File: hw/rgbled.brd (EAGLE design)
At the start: 100 x 80 mm, 17 parts, among them IC1 LE33CZ, Q1 IRLZ34N, Q2 IRLZ34N, Q3 IRLZ34N, U1 ATTINY85-20P, X1 22-23-2021

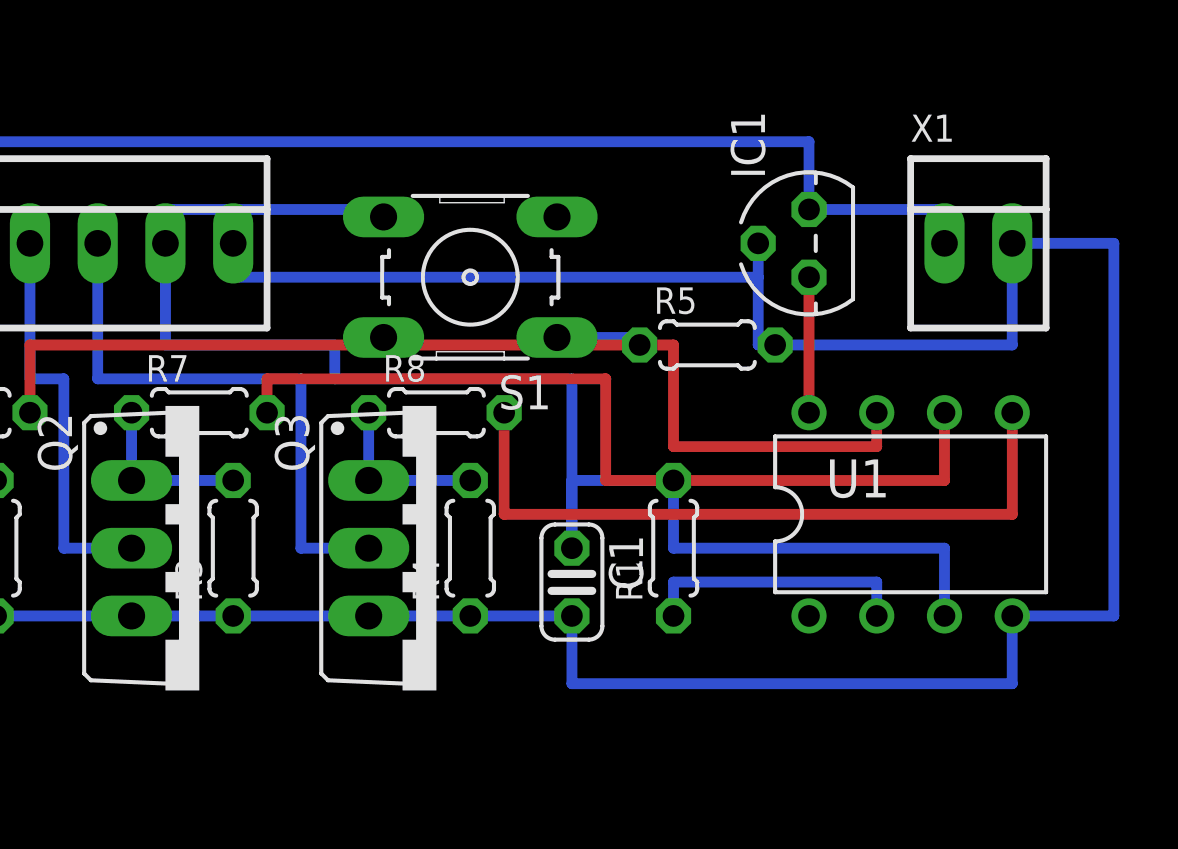
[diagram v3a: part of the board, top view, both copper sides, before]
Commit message: vyhozen dotykovy senzor
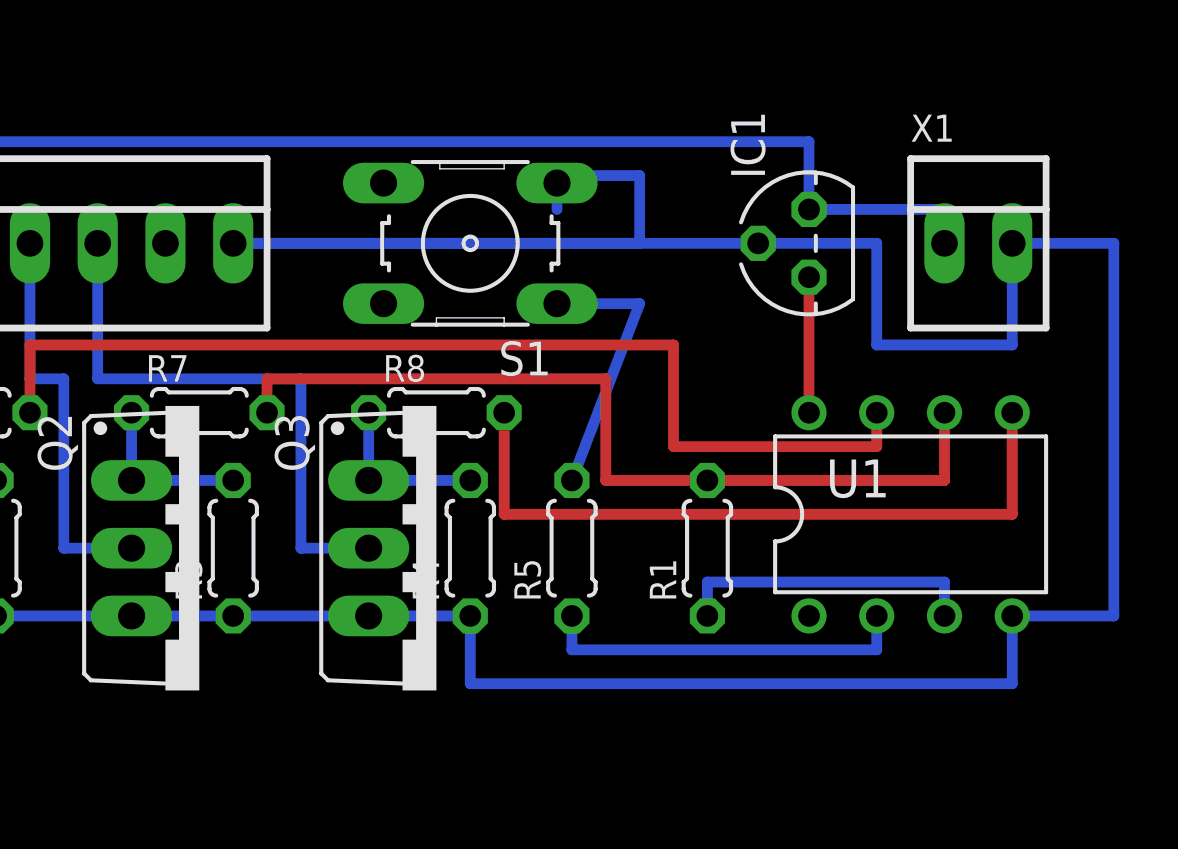
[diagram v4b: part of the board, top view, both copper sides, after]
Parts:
- removed C1: 100p, resistor:C025-024X044
- R1: value 10M -> 4K7
- R5: value 10K -> 4K7
- moved R5 9.16 mm to (30.5, 50.8), turned to 90 degrees
- moved R1 1.27 mm to (35.6, 50.8)
- moved S1 1.27 mm to (26.7, 62.2)
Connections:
- removed net N$7: C1.1, R1.2, S1.3, S1.4, U1.3, X4.5
- new net N$13: R1.2, X4.5
- new net N$14: R5.1, U1.2
- net GND: now also S1.3; no longer C1.2, R5.2
- net N$1: now also R5.2; no longer R5.1, S1.2
- net N$5: now also U1.3; no longer U1.2
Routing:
- net N$7: track 58.0 -> 0.00 mm
- net GND: track 106.7 -> 127.6 mm
- net N$14: track 0.00 -> 14.0 mm
- net N$1: track 3.38 -> 10.2 mm
- net N$5: track 10.2 -> 11.4 mm
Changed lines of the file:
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@@
 </element>
 <element name="IC1" library="linear" package="TO92" value="LE33CZ" x="39.37" y="62.23" rot="R90"/>
-<element name="R1" library="resistor" package="0204/5" value="10M" x="34.29" y="50.8" rot="R90"/>
-<element name="C1" library="resistor" package="C025-024X044" value="100p" x="30.48" y="49.53" rot="R270"/>
 <element name="R2" library="resistor" package="0204/5" value="1M" x="8.89" y="50.8" rot="R90"/>
 <element name="R3" library="resistor" package="0204/5" value="1M" x="17.78" y="50.8" rot="R90"/>
 <element name="R4" library="resistor" package="0204/5" value="1M" x="26.67" y="50.8" rot="R90"/>
-<element name="S1" library="switch-omron" package="B3F-10XX" value="" x="26.67" y="60.96" rot="R180">
-<attribute name="OC_NEWARK" value="36M3542" x="26.67" y="60.96" size="1.778" layer="27" rot="R180" display="off"/>
-<attribute name="MPN" value="B3F-1000" x="26.67" y="60.96" size="1.778" layer="27" rot="R180" display="off"/>
-<attribute name="MF" value="" x="26.67" y="60.96" size="1.778" layer="27" rot="R180" display="off"/>
-<attribute name="OC_FARNELL" value="176432" x="26.67" y="60.96" size="1.778" layer="27" rot="R180" display="off"/>
+<element name="S1" library="switch-omron" package="B3F-10XX" value="" x="26.67" y="62.23" rot="R180">
+<attribute name="OC_NEWARK" value="36M3542" x="26.67" y="62.23" size="1.778" layer="27" rot="R180" display="off"/>
+<attribute name="MPN" value="B3F-1000" x="26.67" y="62.23" size="1.778" layer="27" rot="R180" display="off"/>
+<attribute name="MF" value="" x="26.67" y="62.23" size="1.778" layer="27" rot="R180" display="off"/>
+<attribute name="OC_FARNELL" value="176432" x="26.67" y="62.23" size="1.778" layer="27" rot="R180" display="off"/>
 </element>
-<element name="R5" library="resistor" package="0204/5" value="10K" x="35.56" y="58.42"/>
+<element name="R5" library="resistor" package="0204/5" value="4K7" x="30.48" y="50.8" rot="R90"/>
 <element name="R6" library="resistor" package="0204/5" value="1K" x="7.62" y="55.88"/>
 <element name="R7" library="resistor" package="0204/5" value="1K" x="16.51" y="55.88"/>
 <element name="R8" library="resistor" package="0204/5" value="1K" x="25.4" y="55.88"/>
+<element name="R1" library="resistor" package="0204/5" value="4K7" x="35.56" y="50.8" rot="R90"/>
 </elements>
 <signals>
@@
 <contactref element="Q3" pad="S"/>
 <contactref element="X4" pad="6"/>
-<contactref element="C1" pad="2"/>
 <contactref element="R2" pad="1"/>
 <contactref element="R3" pad="1"/>
 <contactref element="R4" pad="1"/>
-<contactref element="R5" pad="2"/>
 <wire x1="5.08" y1="48.26" x2="8.89" y2="48.26" width="0.4064" layer="16"/>
 <wire x1="8.89" y1="48.26" x2="13.97" y2="48.26" width="0.4064" layer="16"/>
@@
 <wire x1="17.78" y1="48.26" x2="22.86" y2="48.26" width="0.4064" layer="16"/>
 <wire x1="22.86" y1="48.26" x2="26.67" y2="48.26" width="0.4064" layer="16"/>
-<wire x1="26.67" y1="48.26" x2="30.48" y2="48.26" width="0.4064" layer="16"/>
-<wire x1="30.48" y1="48.26" x2="30.48" y2="45.72" width="0.4064" layer="16"/>
-<wire x1="30.48" y1="45.72" x2="46.99" y2="45.72" width="0.4064" layer="16"/>
+<wire x1="26.67" y1="45.72" x2="46.99" y2="45.72" width="0.4064" layer="16"/>
 <wire x1="46.99" y1="45.72" x2="46.99" y2="48.26" width="0.4064" layer="16"/>
 <wire x1="46.99" y1="62.23" x2="50.8" y2="62.23" width="0.4064" layer="16"/>
 <wire x1="50.8" y1="62.23" x2="50.8" y2="48.26" width="0.4064" layer="16"/>
 <wire x1="50.8" y1="48.26" x2="46.99" y2="48.26" width="0.4064" layer="16"/>
-<wire x1="38.1" y1="58.42" x2="46.99" y2="58.42" width="0.4064" layer="16"/>
 <wire x1="46.99" y1="58.42" x2="46.99" y2="62.23" width="0.4064" layer="16"/>
-<wire x1="17.78" y1="62.23" x2="17.78" y2="60.96" width="0.4064" layer="16"/>
-<wire x1="38.1" y1="58.42" x2="37.465" y2="58.42" width="0.4064" layer="16"/>
-<wire x1="37.465" y1="58.42" x2="37.465" y2="60.96" width="0.4064" layer="16"/>
-<wire x1="37.465" y1="60.96" x2="37.465" y2="62.23" width="0.4064" layer="16"/>
-<wire x1="17.78" y1="60.96" x2="37.465" y2="60.96" width="0.4064" layer="16"/>
+<wire x1="17.78" y1="62.23" x2="37.465" y2="62.23" width="0.4064" layer="16"/>
+<wire x1="26.67" y1="48.26" x2="26.67" y2="45.72" width="0.4064" layer="16"/>
+<contactref element="S1" pad="3"/>
+<wire x1="29.9212" y1="63.5" x2="29.9212" y2="64.4906" width="0.4064" layer="16"/>
+<wire x1="37.465" y1="62.23" x2="41.91" y2="62.23" width="0.4064" layer="16"/>
+<wire x1="41.91" y1="62.23" x2="41.91" y2="58.42" width="0.4064" layer="16"/>
+<wire x1="41.91" y1="58.42" x2="46.99" y2="58.42" width="0.4064" layer="16"/>
+<wire x1="17.78" y1="62.23" x2="33.02" y2="62.23" width="0.4064" layer="16"/>
+<wire x1="33.02" y1="62.23" x2="33.02" y2="64.77" width="0.4064" layer="16"/>
+<wire x1="33.02" y1="64.77" x2="29.9212" y2="64.77" width="0.4064" layer="16"/>
+<wire x1="29.9212" y1="64.77" x2="29.9212" y2="64.4906" width="0.4064" layer="16"/>
 </signal>
 <signal name="+12V">
@@
 <wire x1="12.7" y1="57.15" x2="12.7" y2="62.23" width="0.4064" layer="16"/>
 </signal>
-<signal name="N$5">
-<contactref element="U1" pad="2"/>
-<contactref element="R1" pad="1"/>
-<wire x1="34.29" y1="48.26" x2="34.29" y2="49.53" width="0.4064" layer="16"/>
-<wire x1="34.29" y1="49.53" x2="41.91" y2="49.53" width="0.4064" layer="16"/>
-<wire x1="41.91" y1="49.53" x2="41.91" y2="48.26" width="0.4064" layer="16"/>
-</signal>
 <signal name="N$10">
 <contactref element="U1" pad="5"/>
@@
 <wire x1="10.16" y1="58.42" x2="10.16" y2="55.88" width="0.4064" layer="1"/>
 </signal>
-<signal name="N$7">
-<contactref element="R1" pad="2"/>
-<contactref element="C1" pad="1"/>
-<contactref element="X4" pad="5"/>
-<contactref element="U1" pad="3"/>
-<contactref element="S1" pad="3"/>
-<contactref element="S1" pad="4"/>
-<wire x1="23.4188" y1="63.2206" x2="29.9212" y2="63.2206" width="0" layer="19" extent="1-1"/>
-<wire x1="15.24" y1="62.23" x2="15.24" y2="63.5" width="0.4064" layer="16"/>
-<wire x1="15.24" y1="63.5" x2="23.4188" y2="63.5" width="0.4064" layer="16"/>
-<wire x1="23.4188" y1="63.5" x2="23.4188" y2="63.2206" width="0.4064" layer="16"/>
-<wire x1="15.24" y1="62.23" x2="15.24" y2="58.42" width="0.4064" layer="16"/>
-<wire x1="15.24" y1="58.42" x2="21.59" y2="58.42" width="0.4064" layer="16"/>
-<wire x1="21.59" y1="58.42" x2="21.59" y2="57.15" width="0.4064" layer="16"/>
-<wire x1="21.59" y1="57.15" x2="30.48" y2="57.15" width="0.4064" layer="16"/>
-<wire x1="30.48" y1="57.15" x2="30.48" y2="50.8" width="0.4064" layer="16"/>
-<wire x1="44.45" y1="48.26" x2="44.45" y2="50.8" width="0.4064" layer="16"/>
-<wire x1="44.45" y1="50.8" x2="34.29" y2="50.8" width="0.4064" layer="16"/>
-<wire x1="34.29" y1="50.8" x2="34.29" y2="53.34" width="0.4064" layer="16"/>
-<wire x1="34.29" y1="53.34" x2="30.48" y2="53.34" width="0.4064" layer="16"/>
-<wire x1="30.48" y1="53.34" x2="30.48" y2="50.8" width="0.4064" layer="16"/>
-</signal>
-<signal name="N$1">
-<contactref element="S1" pad="1"/>
-<contactref element="R5" pad="1"/>
-<contactref element="S1" pad="2"/>
-<wire x1="23.4188" y1="58.6994" x2="29.9212" y2="58.6994" width="0" layer="19" extent="1-1"/>
-<wire x1="29.9212" y1="58.6994" x2="33.02" y2="58.6994" width="0.4064" layer="16"/>
-<wire x1="33.02" y1="58.6994" x2="33.02" y2="58.42" width="0.4064" layer="16"/>
-</signal>
 <signal name="N$8">
 <contactref element="Q2" pad="G"/>
@@
 <wire x1="5.08" y1="53.34" x2="8.89" y2="53.34" width="0.4064" layer="16"/>
 </signal>
+<signal name="N$5">
+<contactref element="U1" pad="3"/>
+<contactref element="R1" pad="1"/>
+<wire x1="44.45" y1="48.26" x2="44.45" y2="49.53" width="0.4064" layer="16"/>
+<wire x1="44.45" y1="49.53" x2="35.56" y2="49.53" width="0.4064" layer="16"/>
+<wire x1="35.56" y1="49.53" x2="35.56" y2="48.26" width="0.4064" layer="16"/>
+</signal>
+<signal name="N$13">
+<contactref element="R1" pad="2"/>
+<contactref element="X4" pad="5"/>
+<wire x1="35.56" y1="53.34" x2="15.24" y2="62.23" width="0" layer="19" extent="1-1"/>
+</signal>
+<signal name="N$14">
+<contactref element="U1" pad="2"/>
+<contactref element="R5" pad="1"/>
+<wire x1="30.48" y1="48.26" x2="30.48" y2="46.99" width="0.4064" layer="16"/>
+<wire x1="30.48" y1="46.99" x2="41.91" y2="46.99" width="0.4064" layer="16"/>
+<wire x1="41.91" y1="46.99" x2="41.91" y2="48.26" width="0.4064" layer="16"/>
+</signal>
+<signal name="N$1">
+<contactref element="S1" pad="1"/>
+<contactref element="R5" pad="2"/>
+<wire x1="29.9212" y1="59.9694" x2="33.02" y2="59.9694" width="0.4064" layer="16"/>
+<wire x1="33.02" y1="59.9694" x2="30.48" y2="53.34" width="0.4064" layer="16"/>
+</signal>
 </signals>
